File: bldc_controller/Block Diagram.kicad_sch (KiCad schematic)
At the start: 0 parts

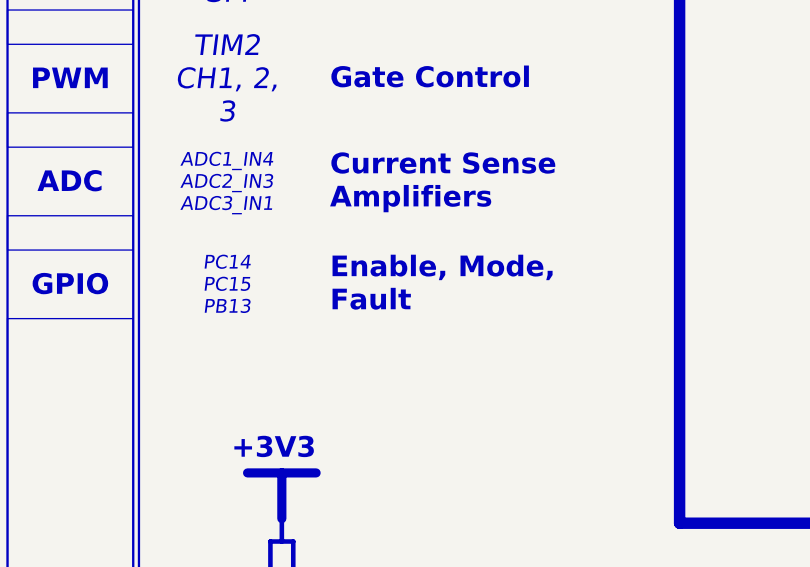
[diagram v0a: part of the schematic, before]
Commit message: schematic is complete. Replaced 5V buck and added pi filters.
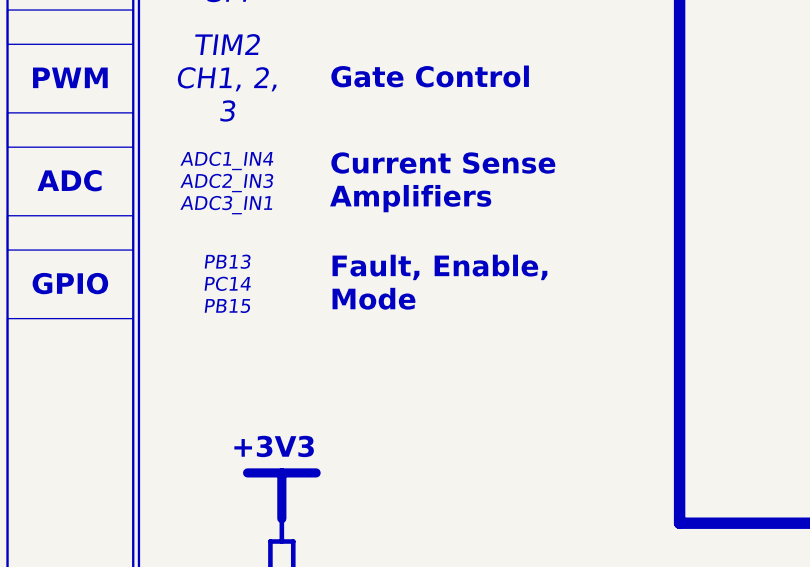
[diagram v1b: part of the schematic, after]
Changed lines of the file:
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@@
   )
   (rectangle (start 46.99 55.88) (end 77.47 71.12)
-    (stroke (width -0.0001) (type default) (color 0 0 0 1))
+    (stroke (width 0) (type default) (color 255 200 0 0.5019607843))
     (fill (type color) (color 255 200 0 0.5019607843))
   )
@@
   )
   (rectangle (start 46.99 151.13) (end 77.47 166.37)
-    (stroke (width -0.0001) (type default) (color 0 0 0 1))
+    (stroke (width 0) (type default) (color 255 200 0 0.5019607843))
     (fill (type color) (color 255 200 0 0.5019607843))
   )
@@
   )
   (rectangle (start 46.99 132.08) (end 77.47 147.32)
-    (stroke (width -0.0001) (type default) (color 0 0 0 1))
+    (stroke (width 0) (type default) (color 255 200 0 0.5019607843))
     (fill (type color) (color 255 200 0 0.5019607843))
   )
@@
   )
   (rectangle (start 46.99 74.93) (end 77.47 90.17)
-    (stroke (width -0.0001) (type default) (color 0 0 0 1))
+    (stroke (width 0) (type default) (color 255 200 0 0.5019607843))
     (fill (type color) (color 255 200 0 0.5019607843))
   )
@@
     (effects (font (face "Times New Roman") (size 2.286 2.286) italic (color 0 0 0 1)))
   )
-  (text_box "Enable, Mode, Fault"
+  (text_box "Fault, Enable, Mode"
     (at 271.526 110.363 0) (size 34.29 10.16)
     (stroke (width -0.0001) (type default))
@@
     (effects (font (face "Arial") (size 2.286 2.286) bold (color 255 255 255 1)) (justify left))
   )
-  (text_box "PC14\nPC15\nPB13"
+  (text_box "PB13\nPC14\nPB15"
     (at 252.73 111.76 0) (size 18.288 7.62)
     (stroke (width -0.0001) (type default))
